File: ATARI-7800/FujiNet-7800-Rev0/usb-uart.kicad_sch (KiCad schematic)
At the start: 15 parts, among them J4 USB-C, U8 CP2102N-A02-GQFN28, U9 UMH3N

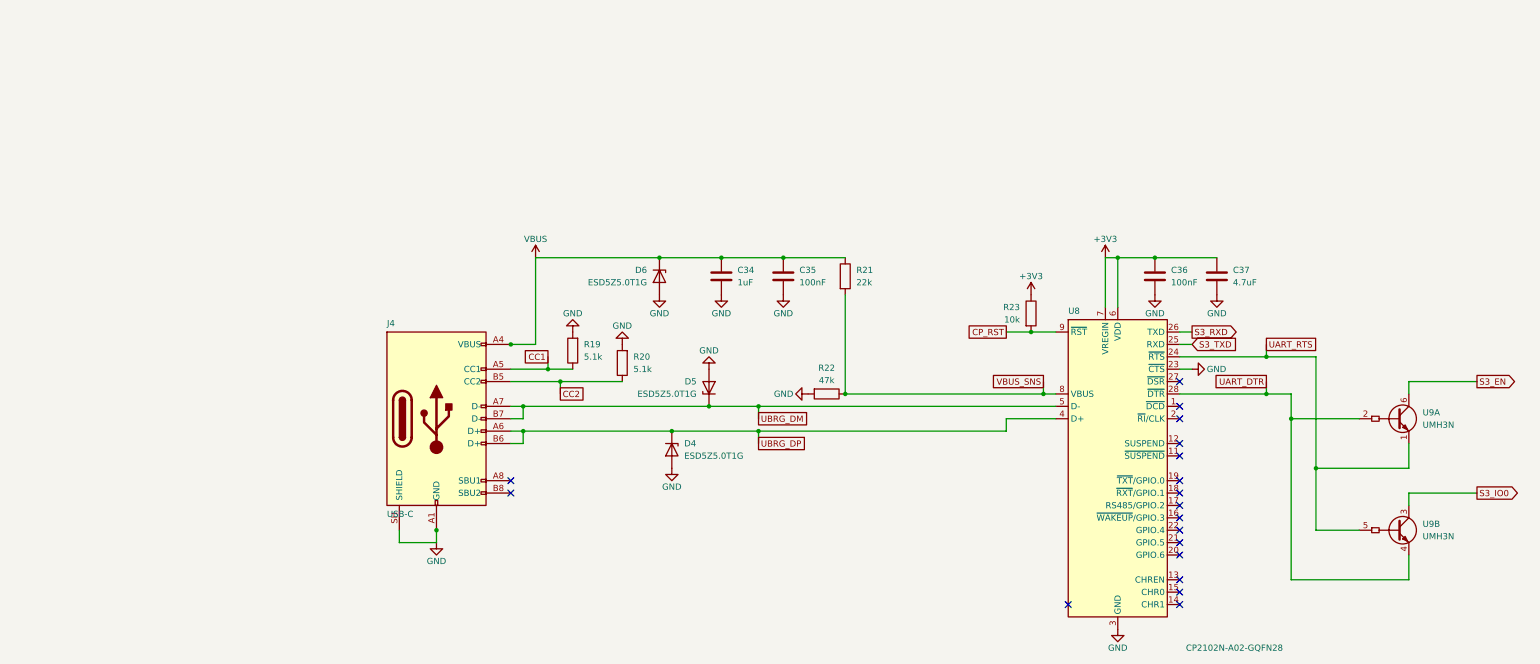
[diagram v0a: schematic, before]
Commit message: ATARI-7800 Rev0: fix the edge, audit the circuit, redraw from the slot, place the board
Edge (board-killer in the schematic-only footprint): the 7800 edge has 18
positions at 2.54 mm with key slots at 3 and 16 for the console's plastic
keys. Pins 1, 2, 15, 16 (and 32, 31, 18, 17) sat one pitch inward, on the
key positions, with no slots and a 42.6 mm tab. tools/edge_geom.py now holds
the geometry (47.0 mm tab, slots centred on +-16.51, 2.4 x 10 mm);
tools/audit/edge_orientation.py checks it against Otaku-flash, tdididit's
boards, the a78-devcart gerbers and this repo's working FujiPlusCart
prototype gerbers (faces and power fingers).

Circuit (console research: Atari C025231 schematic, GCC1702B MARIA spec):
- 4.7k pull-downs on ROM_EN / RAM_EN / A8MASK (RP2350-E9)
- 1k at the /HALT finger (MARIA's HALT is a weak MOS output)
- 10 uF at the console 5V finger; bring-up test pads
- TS-1187A buttons and WS2812C-2020-V1 (the TL3342 and WS2812B-2020
  had 5 in stock at JLC); manufacturer fields for PCBWay
No glue change: R/W is pulled up during MARIA DMA, and the console gates
A15/A14/A12 low while its BIOS is mapped, so CARTSEL never fights it.

Schematic: SMS Rev0's hierarchy (wired root block diagram, hierarchical
labels, netlist parity); sheets in flow order from the slot; the glue
redrawn as a left-to-right gate-depth diagram; references renumbered
from the slot. ERC 0, check_nets 383/383, check_glue 4096/4096.

Board (not yet routed): SMS Rev0's 6-layer pipeline ported. A 72.4 x 115 mm
outline: the stock T-bar width on a 47 x 16.5 mm tab, with the key slots
cut in. Placement variant A (RP over the address fingers, SRAM over the
data fingers): unrouted DRC 0 errors, parity 0, check_vias 0. Shell:
case/FujiNet-7800-Shell.scad. README still describes the old board.

Co-Authored-By: Claude Opus 5.5 <noreply@anthropic.com>
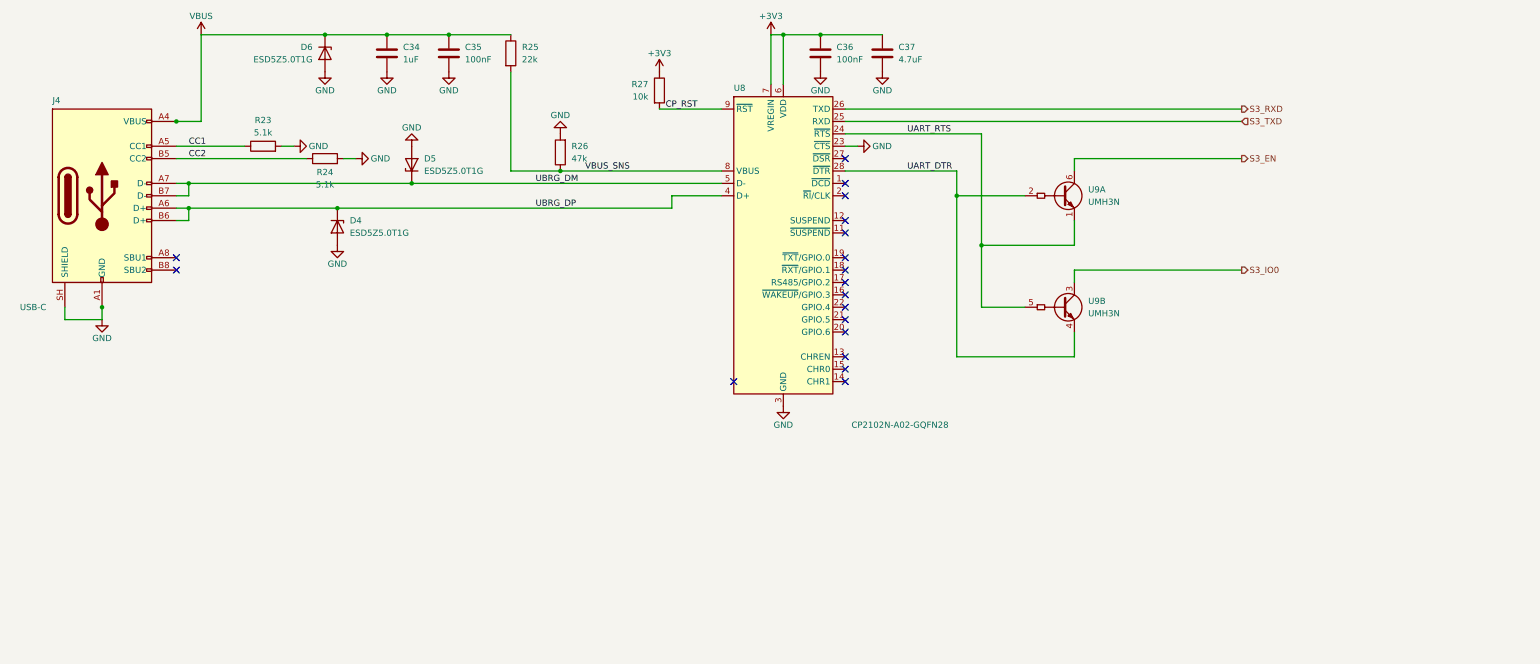
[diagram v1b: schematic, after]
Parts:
- removed R19, R20: 5.1k, FujiNet-7800:R_0603_1608Metric, symbol Device:R
- removed R21: 22k, FujiNet-7800:R_0603_1608Metric, symbol Device:R
- removed R22: 47k, FujiNet-7800:R_0603_1608Metric, symbol Device:R
- added R24: 5.1k, FujiNet-7800:R_0603_1608Metric, symbol Device:R
- added R25: 22k, FujiNet-7800:R_0603_1608Metric, symbol Device:R
- added R26: 47k, FujiNet-7800:R_0603_1608Metric, symbol Device:R
- added R27: 10k, FujiNet-7800:R_0603_1608Metric, symbol Device:R
- R23: value 10k -> 5.1k; LCSC C25804 -> C23186; MPN 0603WAF1002T5E -> 0603WAF5101T5E
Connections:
- net +3V3: now also R27.1; no longer R23.1
- net CC1: now also R23.1
- net CC2: now also R24.1
- net CP_RST: now also R27.2; no longer R23.2
- net GND: now also R23.2, R24.2, R26.2
- net VBUS: now also R25.1
- net VBUS_SNS: now also R25.2, R26.1
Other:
- moved on the sheet: C34, C35, C36, C37, D4, D5, D6, J4, R23, U8, U9A, U9B
